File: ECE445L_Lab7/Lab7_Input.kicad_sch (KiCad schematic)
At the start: 5 parts, among them SW1 UP, SW2 DOWN, SW3 LEFT, SW4 RIGHT, SW5 MODE

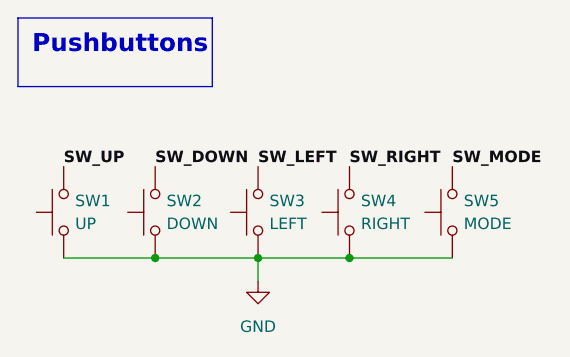
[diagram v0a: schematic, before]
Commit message: update all symbols and re-sync footprints in the KiCad projects
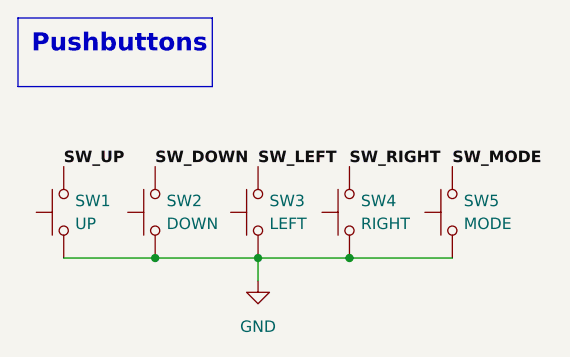
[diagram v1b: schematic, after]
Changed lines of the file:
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@@
 (kicad_sch
-	(version 20231120)
+	(version 20250114)
 	(generator "eeschema")
-	(generator_version "8.0")
+	(generator_version "9.0")
 	(paper "A4")
+	(text_box "Pushbuttons"
+		(exclude_from_sim no)
+		(at 34.925 29.845 0)
+		(size 21.59 7.62)
+		(margins 1.5 1.5 1.5 1.5)
+		(stroke
+			(width 0)
+			(type default)
+		)
+		(fill
+			(type none)
+		)
+		(effects
+			(font
+				(size 2 2)
+				(thickness 0.4)
+				(bold yes)
+			)
+			(justify left top)
+		)
+	)
 	(junction
 		(at 50.165 56.515)
@@
 		)
 	)
-	(text_box "Pushbuttons"
-		(exclude_from_sim no)
-		(at 34.925 29.845 0)
-		(size 21.59 7.62)
-		(stroke
-			(width 0)
-			(type default)
-		)
-		(fill
-			(type none)
-		)
-		(effects
-			(font
-				(size 2 2)
-				(thickness 0.4)
-				(bold yes)
-			)
-			(justify left top)
-		)
-	)
 	(label "SW_RIGHT"
 		(at 71.755 46.355 0)
-		(fields_autoplaced yes)
 		(effects
 			(font
@@
 	(label "SW_MODE"
 		(at 83.185 46.355 0)
-		(fields_autoplaced yes)
 		(effects
 			(font
@@
 	(label "SW_DOWN"
 		(at 50.165 46.355 0)
-		(fields_autoplaced yes)
 		(effects
 			(font
@@
 	(label "SW_LEFT"
 		(at 61.595 46.355 0)
-		(fields_autoplaced yes)
 		(effects
 			(font
@@
 	(label "SW_UP"
 		(at 40.005 46.355 0)
-		(fields_autoplaced yes)
 		(effects
 			(font
